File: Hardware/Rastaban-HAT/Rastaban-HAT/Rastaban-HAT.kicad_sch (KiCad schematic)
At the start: 61 parts, among them J10 GPIO, J11 Conn_01x06_Male, J4 Screw_Terminal_01x02, J5 Jack-DC 12V+, J6 SM04B-SRSS-TB(LF)(SN), J7 Screw_Terminal_01x02, J8 Screw_Terminal_01x02, J9 Conn_01x05_Male, M1 Fan, Q1 2N7002K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

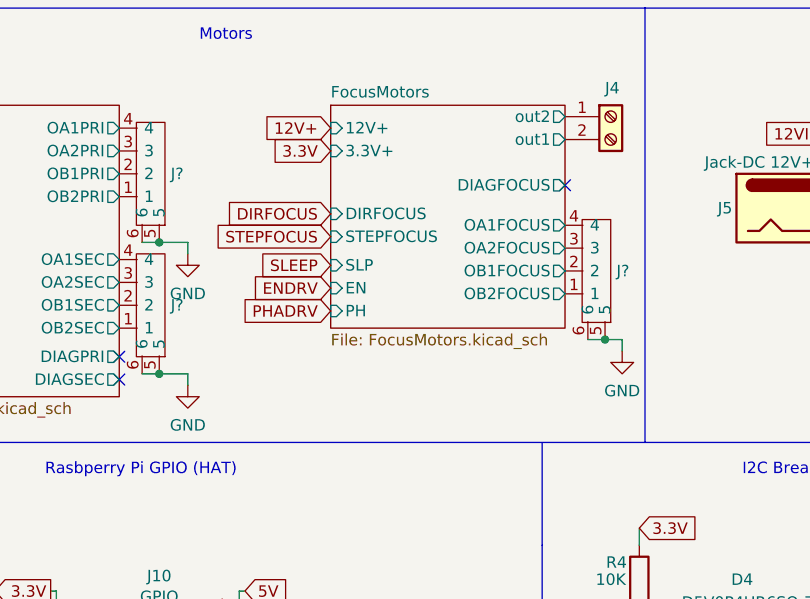
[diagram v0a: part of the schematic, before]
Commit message: added connector footprint to schematic
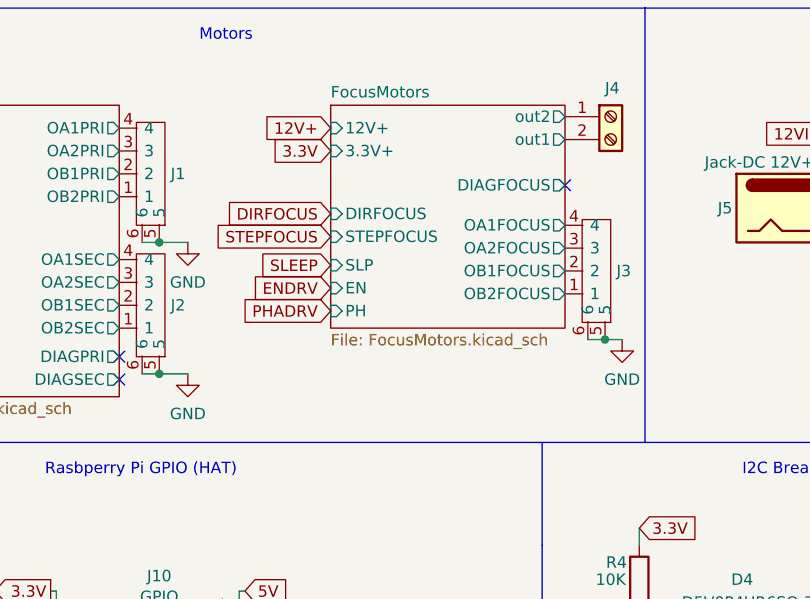
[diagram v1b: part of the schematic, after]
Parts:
- D1, D4: footprint SOT95P285X140-6N -> (none)
- J1, J2, J3: renamed from J?; footprint 1778780 -> SmacSYs:1778780
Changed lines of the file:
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@@
     (stroke (width 0) (type solid) (color 0 0 0 0))
-  )
-  (wire (pts (xy 131.445 53.34) (xy 131.445 54.61))
-    (stroke (width 0) (type default) (color 0 0 0 0))
   )
   (wire (pts (xy 227.33 45.085) (xy 227.33 55.245))
@@
     (stroke (width 0) (type default) (color 0 0 0 0))
   )
-  (wire (pts (xy 179.705 49.53) (xy 179.705 50.8))
-    (stroke (width 0) (type default) (color 0 0 0 0))
-  )
   (wire (pts (xy 116.205 77.47) (xy 116.84 77.47))
     (stroke (width 0) (type default) (color 0 0 0 0))
@@
   )
   (wire (pts (xy 205.105 32.385) (xy 206.248 32.385))
-    (stroke (width 0) (type default) (color 0 0 0 0))
-  )
-  (wire (pts (xy 131.445 38.735) (xy 131.445 40.005))
     (stroke (width 0) (type default) (color 0 0 0 0))
   )
@@
   (symbol (lib_name "1778780_1") (lib_id "SamacSys_Parts:1778780") (at 130.81 31.75 180) (unit 1)
     (in_bom yes) (on_board yes) (fields_autoplaced)
-    (property "Reference" "J?" (id 0) (at 129.54 31.1149 0)
+    (property "Reference" "J1" (id 0) (at 129.54 31.1149 0)
       (effects (font (size 1.27 1.27)) (justify right))
     )
@@
       (effects (font (size 1.27 1.27)) (justify right) hide)
     )
-    (property "Footprint" "1778780" (id 2) (at 138.43 23.495 0)
+    (property "Footprint" "SmacSYs:1778780" (id 2) (at 138.43 23.495 0)
       (effects (font (size 1.27 1.27)) (justify left) hide)
     )
@@
   (symbol (lib_name "1778780_1") (lib_id "SamacSys_Parts:1778780") (at 130.81 46.355 180) (unit 1)
     (in_bom yes) (on_board yes) (fields_autoplaced)
-    (property "Reference" "J?" (id 0) (at 129.54 45.7199 0)
+    (property "Reference" "J2" (id 0) (at 129.54 45.7199 0)
       (effects (font (size 1.27 1.27)) (justify right))
     )
@@
       (effects (font (size 1.27 1.27)) (justify right) hide)
     )
-    (property "Footprint" "1778780" (id 2) (at 138.43 38.1 0)
+    (property "Footprint" "SmacSYs:1778780" (id 2) (at 138.43 38.1 0)
       (effects (font (size 1.27 1.27)) (justify left) hide)
     )
@@
     (property "Reference" "D4" (id 0) (at 193.04 76.2 0))
     (property "Value" "D5V0P4UR6SO-7" (id 1) (at 193.675 78.74 0))
-    (property "Footprint" "SOT95P285X140-6N" (id 2) (at 180.34 107.315 0)
+    (property "Footprint" "" (id 2) (at 180.34 107.315 0)
       (effects (font (size 1.27 1.27)) (justify left) hide)
     )
@@
     (pin "1")
   )
-  (symbol (lib_id "power:GND") (at 131.445 54.61 0) (unit 1)
+  (symbol (lib_id "power:GND") (at 131.445 53.34 0) (unit 1)
     (in_bom yes) (on_board yes) (fields_autoplaced)
-    (property "Reference" "#PWR?" (id 0) (at 131.445 60.96 0)
-      (effects (font (size 1.27 1.27)) hide)
-    )
-    (property "Value" "GND" (id 1) (at 131.445 59.055 0))
-    (property "Footprint" "" (id 2) (at 131.445 54.61 0)
-      (effects (font (size 1.27 1.27)) hide)
-    )
-    (property "Datasheet" "" (id 3) (at 131.445 54.61 0)
+    (property "Reference" "#PWR025" (id 0) (at 131.445 59.69 0)
+      (effects (font (size 1.27 1.27)) hide)
+    )
+    (property "Value" "GND" (id 1) (at 131.445 57.785 0))
+    (property "Footprint" "" (id 2) (at 131.445 53.34 0)
+      (effects (font (size 1.27 1.27)) hide)
+    )
+    (property "Datasheet" "" (id 3) (at 131.445 53.34 0)
       (effects (font (size 1.27 1.27)) hide)
     )
@@
   (symbol (lib_name "1778780_1") (lib_id "SamacSys_Parts:1778780") (at 180.34 42.545 180) (unit 1)
     (in_bom yes) (on_board yes)
-    (property "Reference" "J?" (id 0) (at 179.07 41.9099 0)
+    (property "Reference" "J3" (id 0) (at 179.07 41.9099 0)
       (effects (font (size 1.27 1.27)) (justify right))
     )
@@
       (effects (font (size 1.27 1.27)) (justify right) hide)
     )
-    (property "Footprint" "1778780" (id 2) (at 187.96 34.29 0)
+    (property "Footprint" "SmacSYs:1778780" (id 2) (at 187.96 34.29 0)
       (effects (font (size 1.27 1.27)) (justify left) hide)
     )
@@
     (property "Reference" "D1" (id 0) (at 192.405 127 0))
     (property "Value" "D5V0P4UR6SO-7" (id 1) (at 193.04 129.54 0))
-    (property "Footprint" "SOT95P285X140-6N" (id 2) (at 179.705 158.115 0)
+    (property "Footprint" "" (id 2) (at 179.705 158.115 0)
       (effects (font (size 1.27 1.27)) (justify left) hide)
     )
@@
     (pin "2")
   )
-  (symbol (lib_id "power:GND") (at 179.705 50.8 0) (unit 1)
-    (in_bom yes) (on_board yes)
-    (property "Reference" "#PWR?" (id 0) (at 179.705 57.15 0)
-      (effects (font (size 1.27 1.27)) hide)
-    )
-    (property "Value" "GND" (id 1) (at 179.705 55.245 0))
-    (property "Footprint" "" (id 2) (at 179.705 50.8 0)
-      (effects (font (size 1.27 1.27)) hide)
-    )
-    (property "Datasheet" "" (id 3) (at 179.705 50.8 0)
+  (symbol (lib_id "power:GND") (at 179.705 49.53 0) (unit 1)
+    (in_bom yes) (on_board yes)
+    (property "Reference" "#PWR026" (id 0) (at 179.705 55.88 0)
+      (effects (font (size 1.27 1.27)) hide)
+    )
+    (property "Value" "GND" (id 1) (at 179.705 53.975 0))
+    (property "Footprint" "" (id 2) (at 179.705 49.53 0)
+      (effects (font (size 1.27 1.27)) hide)
+    )
+    (property "Datasheet" "" (id 3) (at 179.705 49.53 0)
       (effects (font (size 1.27 1.27)) hide)
     )
@@
     (pin "1")
   )
-  (symbol (lib_id "power:GND") (at 131.445 40.005 0) (unit 1)
+  (symbol (lib_id "power:GND") (at 131.445 38.735 0) (unit 1)
     (in_bom yes) (on_board yes) (fields_autoplaced)
-    (property "Reference" "#PWR?" (id 0) (at 131.445 46.355 0)
-      (effects (font (size 1.27 1.27)) hide)
-    )
-    (property "Value" "GND" (id 1) (at 131.445 44.45 0))
-    (property "Footprint" "" (id 2) (at 131.445 40.005 0)
-      (effects (font (size 1.27 1.27)) hide)
-    )
-    (property "Datasheet" "" (id 3) (at 131.445 40.005 0)
+    (property "Reference" "#PWR07" (id 0) (at 131.445 45.085 0)
+      (effects (font (size 1.27 1.27)) hide)
+    )
+    (property "Value" "GND" (id 1) (at 131.445 43.18 0))
+    (property "Footprint" "" (id 2) (at 131.445 38.735 0)
+      (effects (font (size 1.27 1.27)) hide)
+    )
+    (property "Datasheet" "" (id 3) (at 131.445 38.735 0)
       (effects (font (size 1.27 1.27)) hide)
     )
@@
       (reference "#PWR06") (unit 1) (value "GND") (footprint "")
     )
+    (path "/f05b184b-1c9b-4874-a5bb-12e0b571204c"
+      (reference "#PWR07") (unit 1) (value "GND") (footprint "")
+    )
     (path "/e584f539-ed06-4cdc-9218-25b6d9e804f7"
       (reference "#PWR08") (unit 1) (value "GND") (footprint "")
@@
       (reference "#PWR024") (unit 1) (value "GND") (footprint "")
     )
+    (path "/7feab395-fd73-4cd2-af00-f8505afbf50b"
+      (reference "#PWR025") (unit 1) (value "GND") (footprint "")
+    )
+    (path "/e42dbb93-2d19-450f-8bca-f4e8b2381adb"
+      (reference "#PWR026") (unit 1) (value "GND") (footprint "")
+    )
     (path "/0e27d84c-7f28-4ae1-bfb4-dddd948392f2"
       (reference "#PWR0132") (unit 1) (value "+3.3V") (footprint "")
@@
       (reference "#PWR0133") (unit 1) (value "+3.3V") (footprint "")
     )
-    (path "/7feab395-fd73-4cd2-af00-f8505afbf50b"
-      (reference "#PWR?") (unit 1) (value "GND") (footprint "")
-    )
-    (path "/e42dbb93-2d19-450f-8bca-f4e8b2381adb"
-      (reference "#PWR?") (unit 1) (value "GND") (footprint "")
-    )
-    (path "/f05b184b-1c9b-4874-a5bb-12e0b571204c"
-      (reference "#PWR?") (unit 1) (value "GND") (footprint "")
-    )
     (path "/f3fe5026-3ec3-4ef9-8ee4-ac53381f5d3c"
       (reference "C1") (unit 1) (value "10u 10V") (footprint "")
@@
     )
     (path "/9133e68d-23af-46c3-8c54-85262a40fe4d"
-      (reference "D1") (unit 1) (value "D5V0P4UR6SO-7") (footprint "SOT95P285X140-6N")
+      (reference "D1") (unit 1) (value "D5V0P4UR6SO-7") (footprint "")
     )
     (path "/f3747824-7ae0-46af-a774-78fceec77b76"
@@
     )
     (path "/6578ccc9-8e10-4703-a403-8d3952656fca"
-      (reference "D4") (unit 1) (value "D5V0P4UR6SO-7") (footprint "SOT95P285X140-6N")
+      (reference "D4") (unit 1) (value "D5V0P4UR6SO-7") (footprint "")
     )
     (path "/bacc34b0-9755-45d5-8946-44f33e8699fb"
@@
       (reference "IC2") (unit 1) (value "DMMT5401-7-F") (footprint "SmacSYs:SOT95P285X140-6N")
     )
+    (path "/3e10c08e-67b3-4717-b449-44243f0aae62"
+      (reference "J1") (unit 1) (value "1778780") (footprint "SmacSYs:1778780")
+    )
+    (path "/50b07640-10d9-48fc-9f46-0d336057ad58"
+      (reference "J2") (unit 1) (value "1778780") (footprint "SmacSYs:1778780")
+    )
+    (path "/87d14d87-71bb-4442-8b22-a0d69c5e1e74"
+      (reference "J3") (unit 1) (value "1778780") (footprint "SmacSYs:1778780")
+    )
     (path "/5aac9ea9-4fe8-4ec4-82c6-ee5bf07b1349"
       (reference "J4") (unit 1) (value "Screw_Terminal_01x02") (footprint "TerminalBlock:TerminalBlock_Altech_AK300-2_P5.00mm")
@@
       (reference "J11") (unit 1) (value "Conn_01x06_Male") (footprint "Connector_PinSocket_2.54mm:PinSocket_1x06_P2.54mm_Vertical")
     )
-    (path "/3e10c08e-67b3-4717-b449-44243f0aae62"
-      (reference "J?") (unit 1) (value "1778780") (footprint "1778780")
-    )
-    (path "/50b07640-10d9-48fc-9f46-0d336057ad58"
-      (reference "J?") (unit 1) (value "1778780") (footprint "1778780")
-    )
-    (path "/87d14d87-71bb-4442-8b22-a0d69c5e1e74"
-      (reference "J?") (unit 1) (value "1778780") (footprint "1778780")
-    )
     (path "/d76e85fc-4f2e-4d54-b404-7aa3a9abd669"

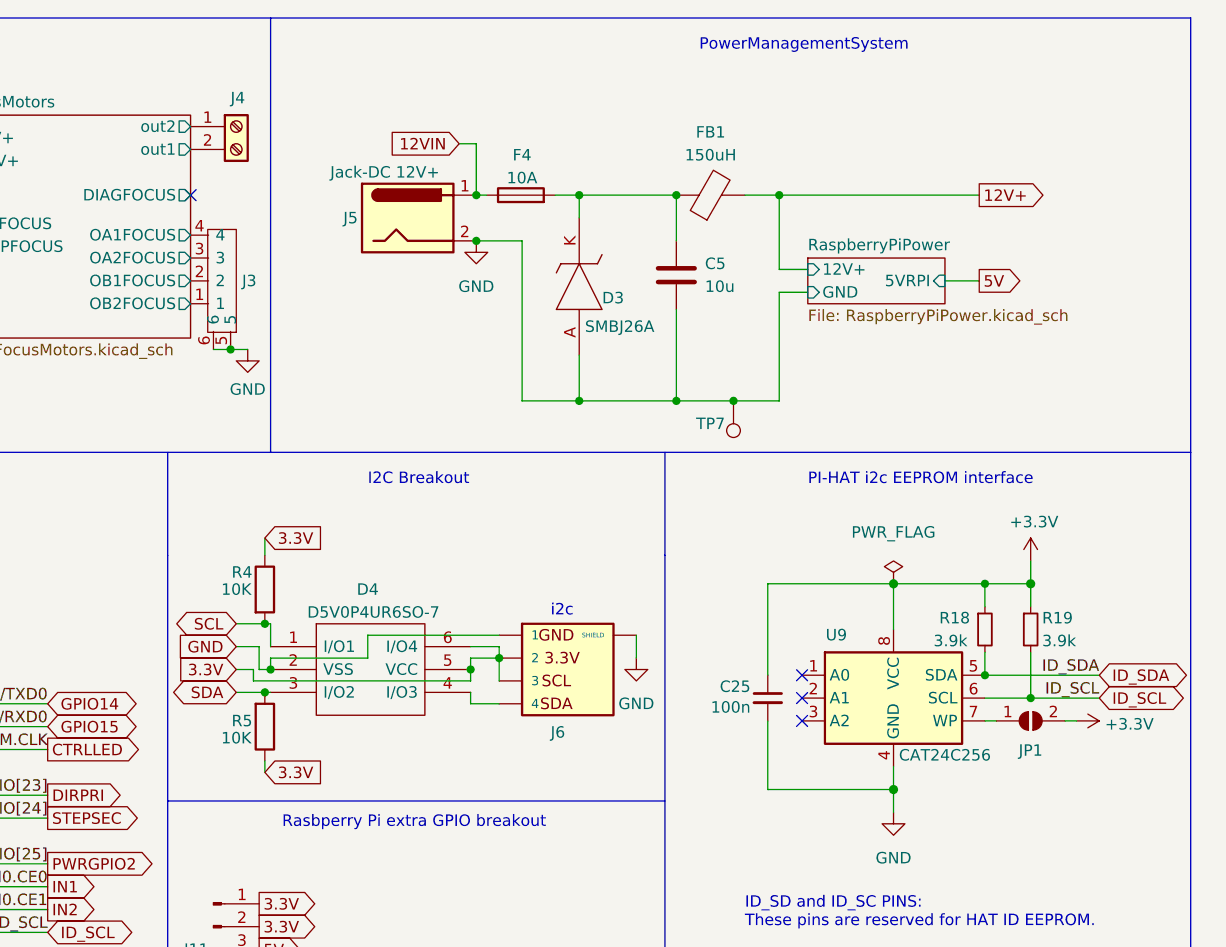
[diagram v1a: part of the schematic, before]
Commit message: fixed eeprom esd protection
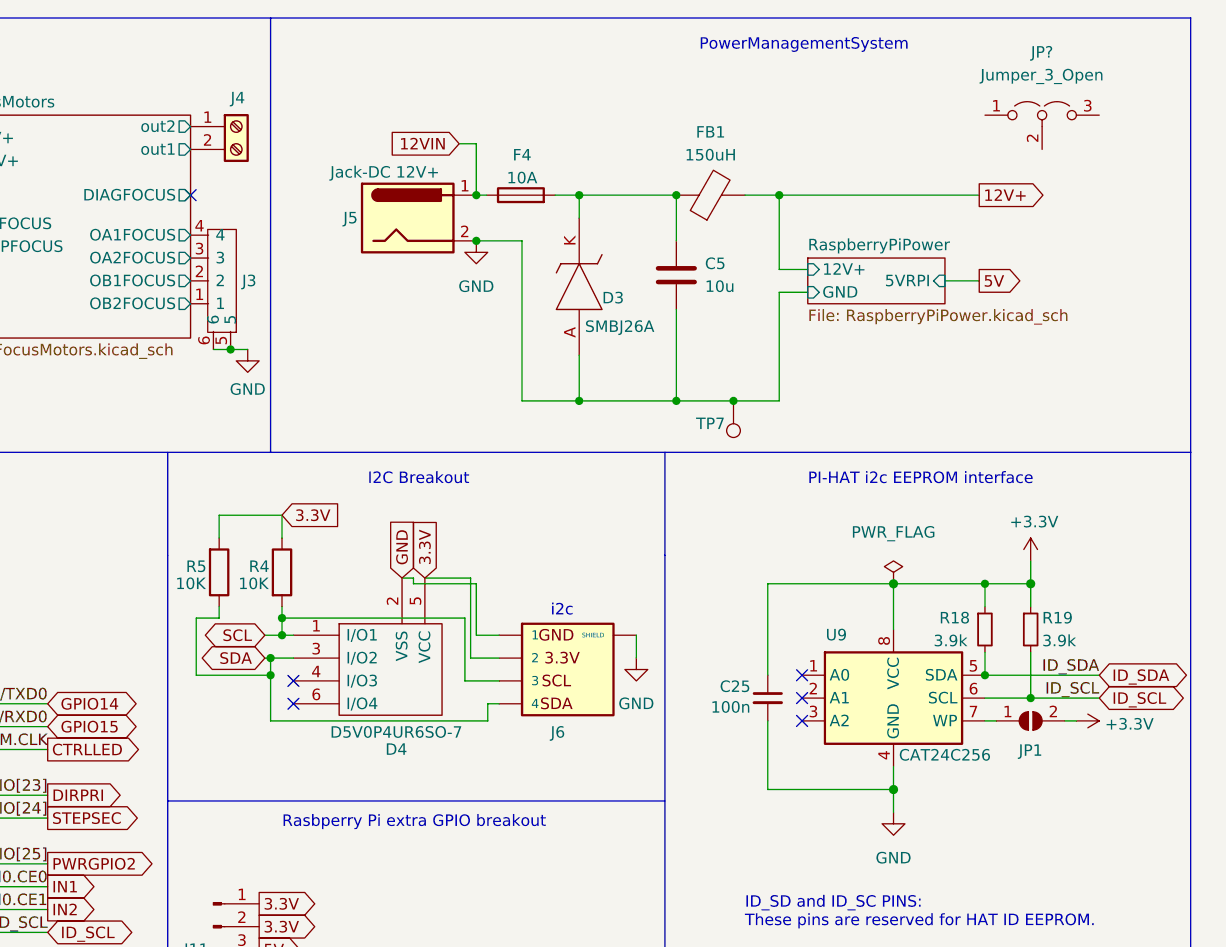
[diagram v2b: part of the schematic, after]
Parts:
- added JP?: Jumper_3_Open, symbol Jumper:Jumper_3_Open
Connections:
- net 3.3V: now also R5.2; no longer D4.6 (I/O4), J6.3, R5.1
- net SCL: now also J6.3
- net SDA: now also J6.4, R5.1; no longer R5.2
- net at D4.4 (I/O3): no longer J6.4
- no-connect marks 6 -> 8
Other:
- moved on the sheet: D4, R4, R5

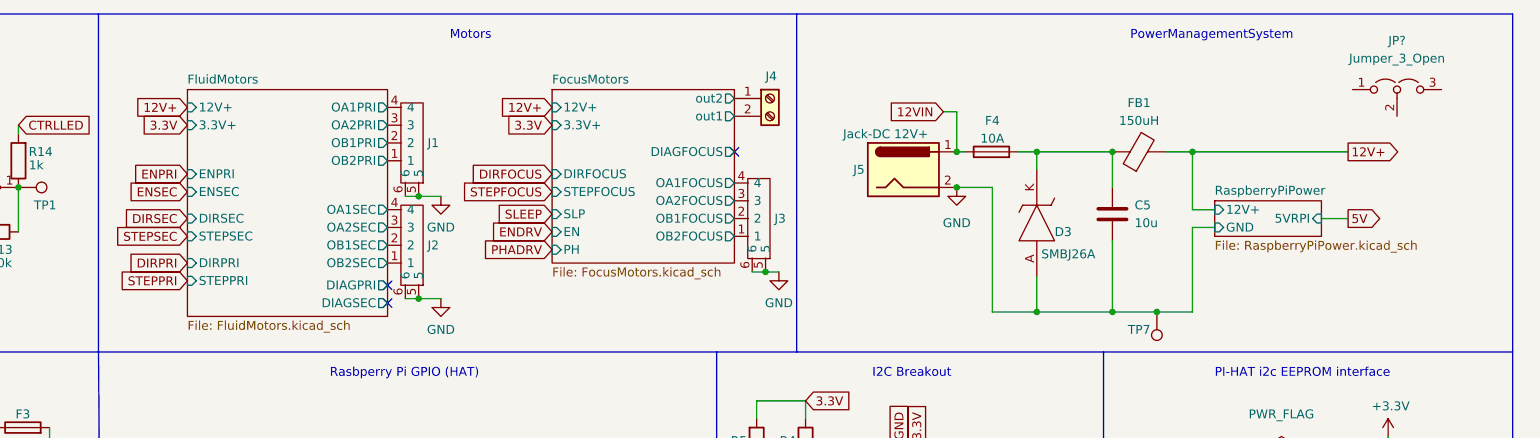
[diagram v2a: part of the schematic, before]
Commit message: added 24V+ supply jumpers to prim and sec motors
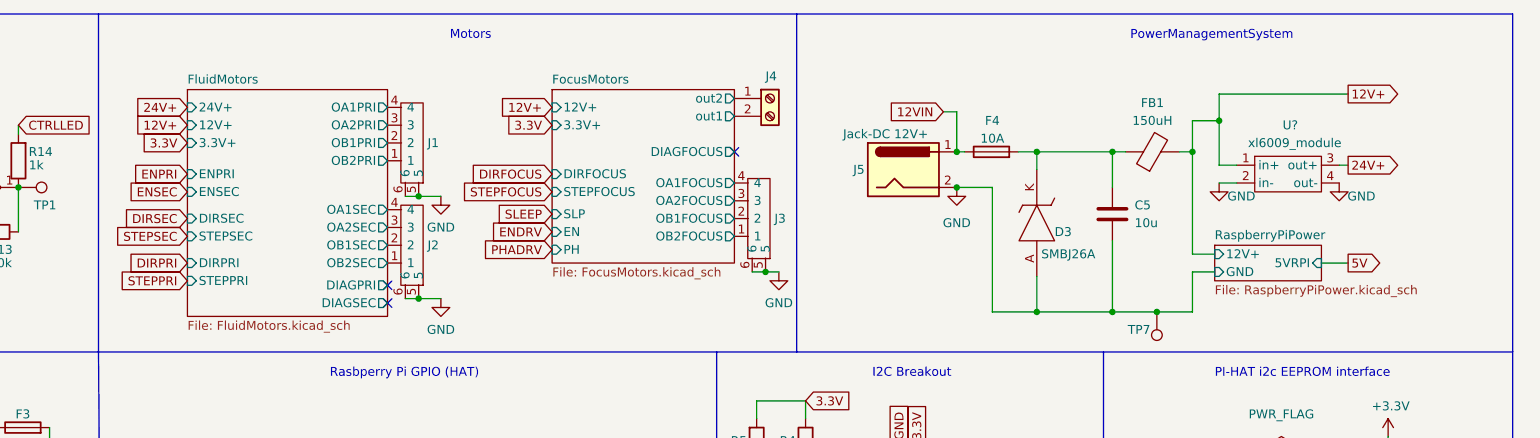
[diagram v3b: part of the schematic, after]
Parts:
- removed JP?: Jumper_3_Open, symbol Jumper:Jumper_3_Open
- added U?: xl6009_module, symbol Battery_Management:xl6009_module
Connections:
- net 12V+: now also U?.1 (in+)
- net GND: now also U?.2 (in-), U?.4 (out-)
- new net 24V+: U?.3 (out+)
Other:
- sheet FluidMotors ports: added 24V+; removed none
- moved on the sheet: FB1

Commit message: enh layout
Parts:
- gave numbers to parts that had none: 1
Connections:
- net +3V3: no longer C25.1, R18.1, R19.1, U9.8 (VCC)
- net 3.3V renamed 3.3V+
- net 3.3V+: now also C25.1, R18.1, R19.1, U9.8 (VCC)
- net 5V renamed 5V+

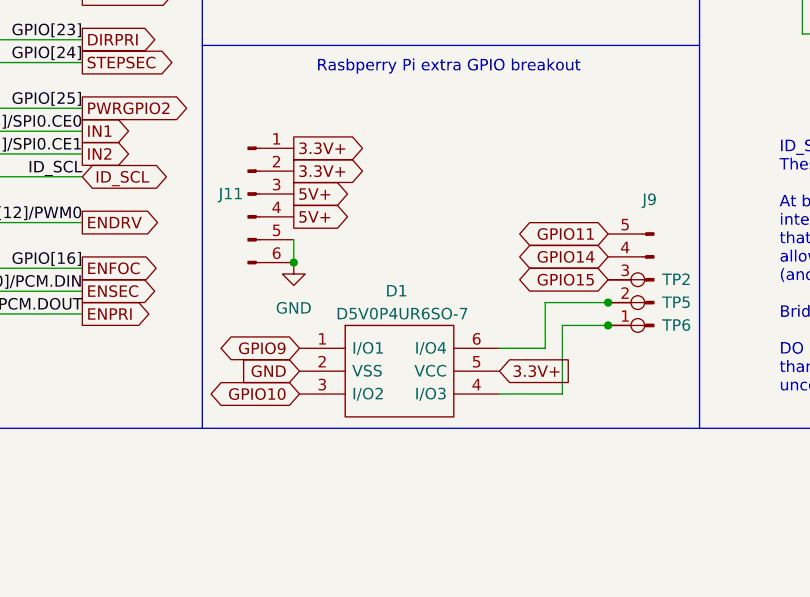
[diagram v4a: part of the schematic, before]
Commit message: added GPIO esd protection
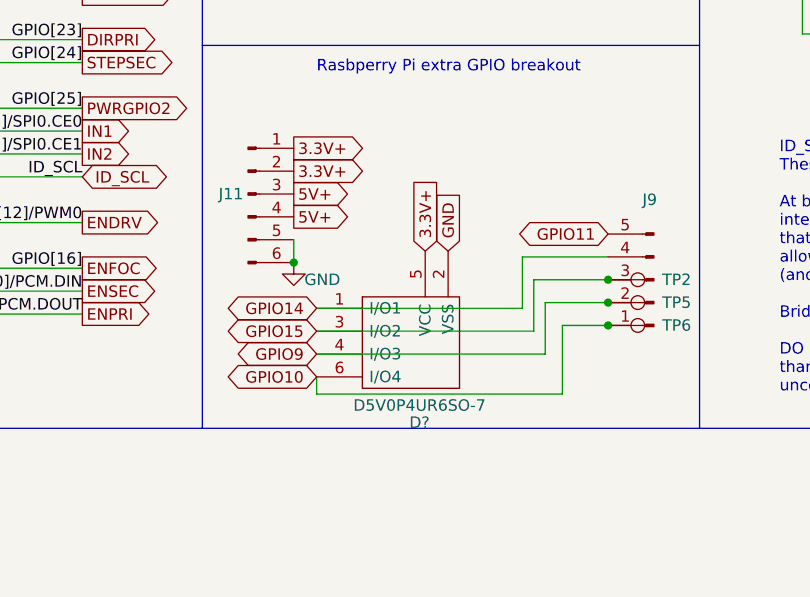
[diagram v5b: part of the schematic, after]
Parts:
- removed D1: D5V0P4UR6SO-7, symbol SamacSys_Parts:D5V0P4UR6SO-7
- added D?: D5V0P4UR6SO-7, symbol SamacSys_Parts:D5V0P4UR6SO-7
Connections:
- net 3.3V+: now also D?.5 (VCC)
- net GND: now also D?.2 (VSS)
- net GPIO10: now also J9.1 (Pin_1), TP6.1, D?.6 (I/O4)
- net GPIO14: now also D?.1 (I/O1)
- net GPIO15: now also D?.3 (I/O2)
- net GPIO9: now also J9.2 (Pin_2), TP5.1, D?.4 (I/O3)
